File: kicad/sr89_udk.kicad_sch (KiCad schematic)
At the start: 5 parts

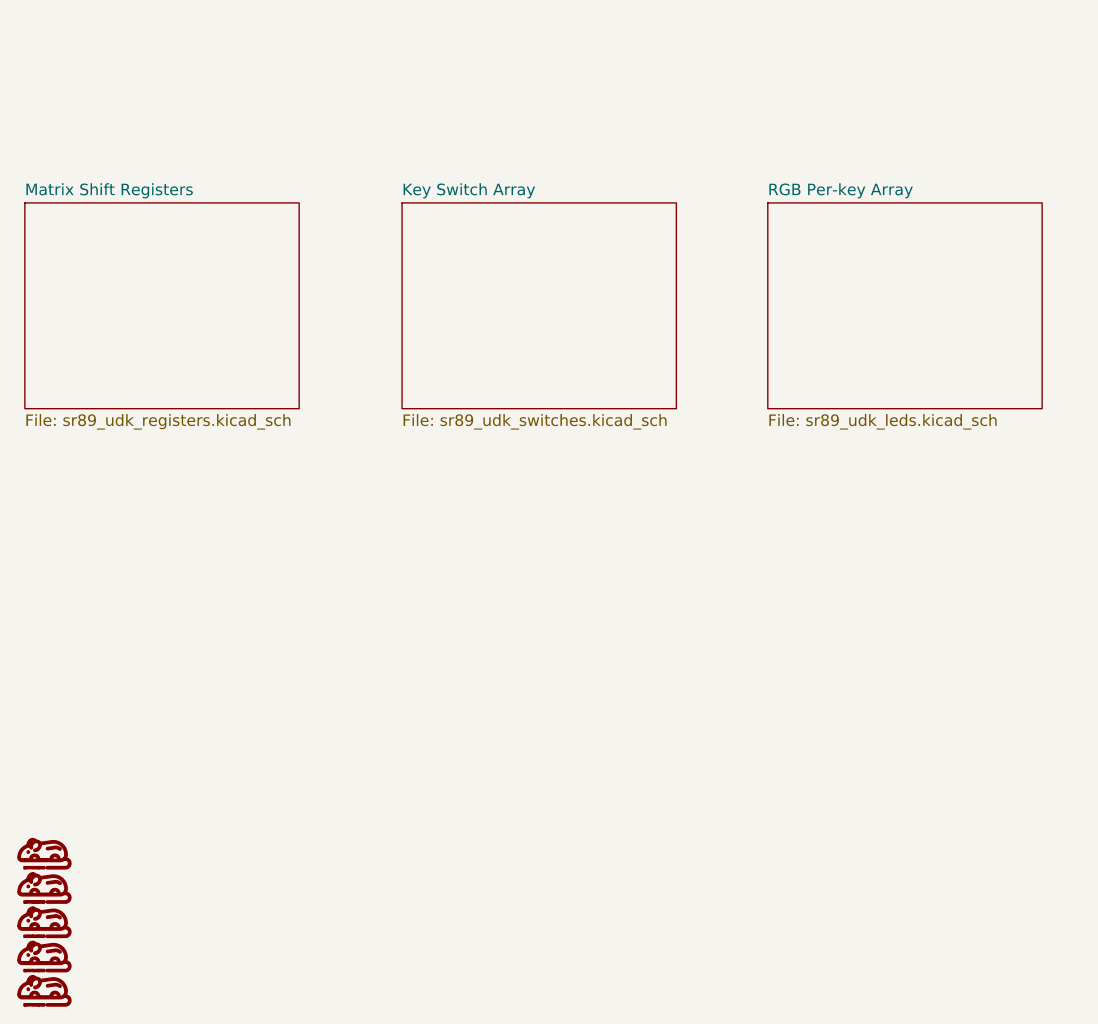
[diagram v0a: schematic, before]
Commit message: routed, but not rules checked
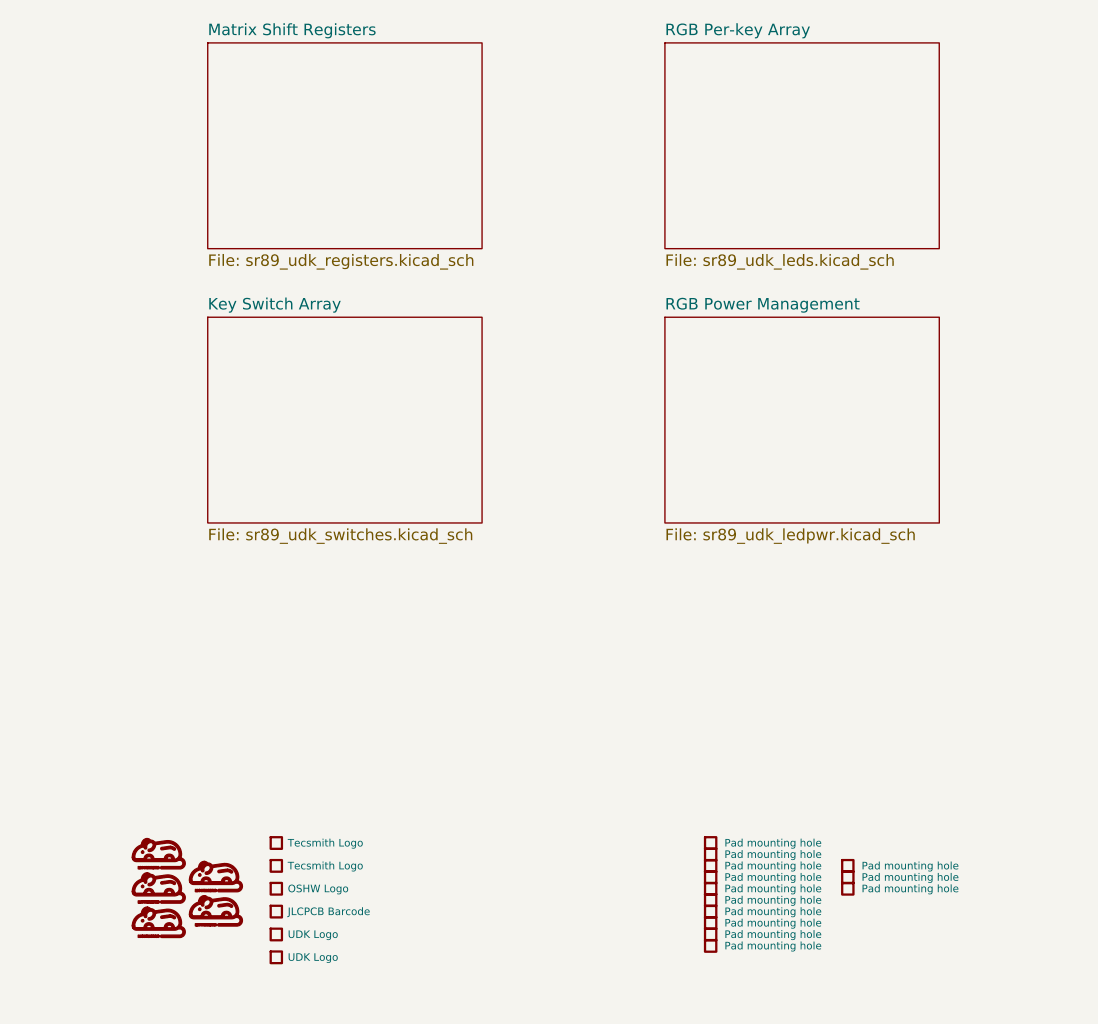
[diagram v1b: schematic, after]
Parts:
- added MT_{2}1, MT_{2}10, MT_{2}11, MT_{2}12, MT_{2}13, MT_{2}2, MT_{2}3, MT_{2}4, MT_{2}5, MT_{2}6, MT_{2}7, MT_{2}8, MT_{2}9: Pad mounting hole, 0_sr89:MountingHole_2.2mm_M2_ISO14580, symbol ts-kicad-lib:X
- added X1, X2: Tecsmith Logo, ts-logos-lib:Tecsmith_20mm, symbol ts-kicad-lib:X
- added X3: OSHW Logo, Symbol:OSHW-Logo_7.5x8mm_SilkScreen, symbol ts-kicad-lib:X
- added X4: JLCPCB Barcode, ts-jlcpcb-lib:jlcpcb_order_number_5x5, symbol ts-kicad-lib:X
- added X5, X6: UDK Logo, ts-logos-lib:UDK_5mm, symbol ts-kicad-lib:X
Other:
- added sheet RGB Power Management (sr89_udk_ledpwr.kicad_sch)
